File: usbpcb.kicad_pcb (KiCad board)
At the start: 2 copper layers, 32.5 x 56 mm, 6 parts, among them J1 USB_A, J2 USB3_A, J3 Conn_02x05_Counter_Clockwise, J4 Conn_02x05_Counter_Clockwise

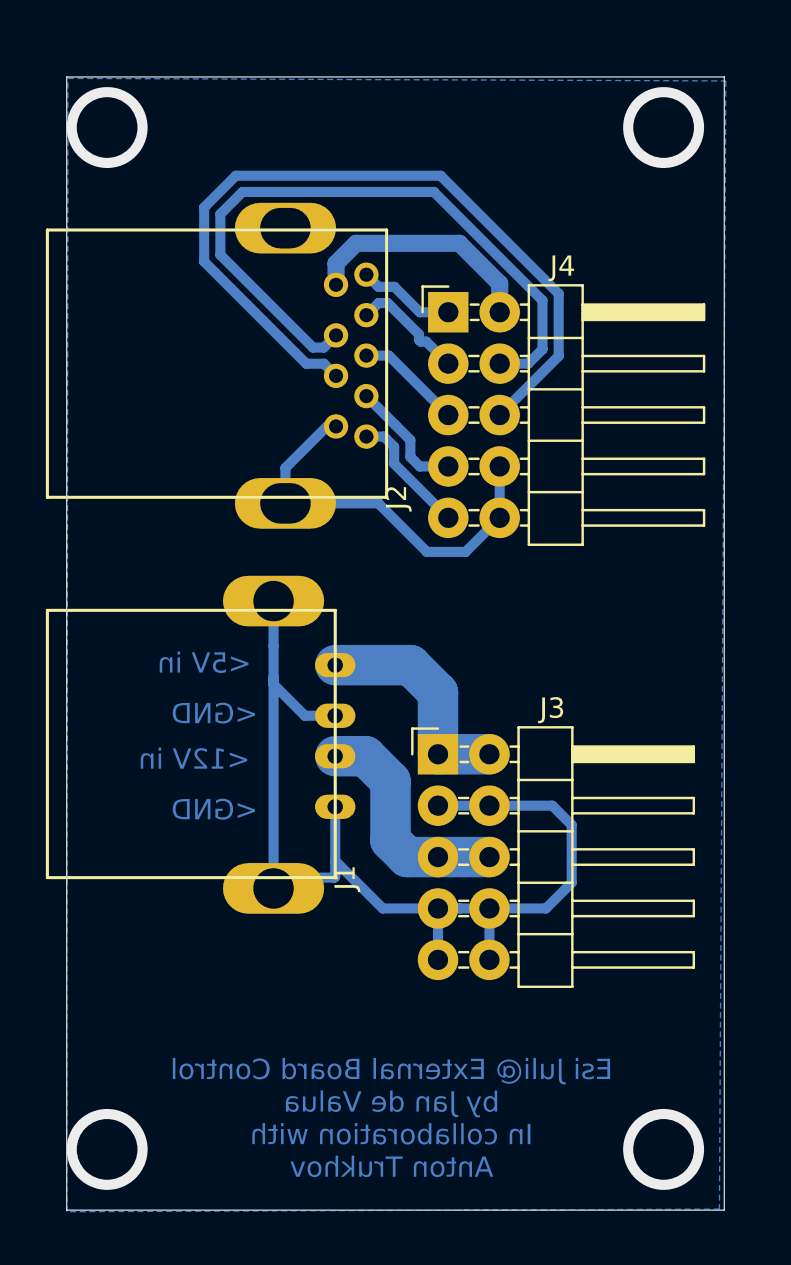
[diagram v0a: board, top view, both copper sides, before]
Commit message: update after fail
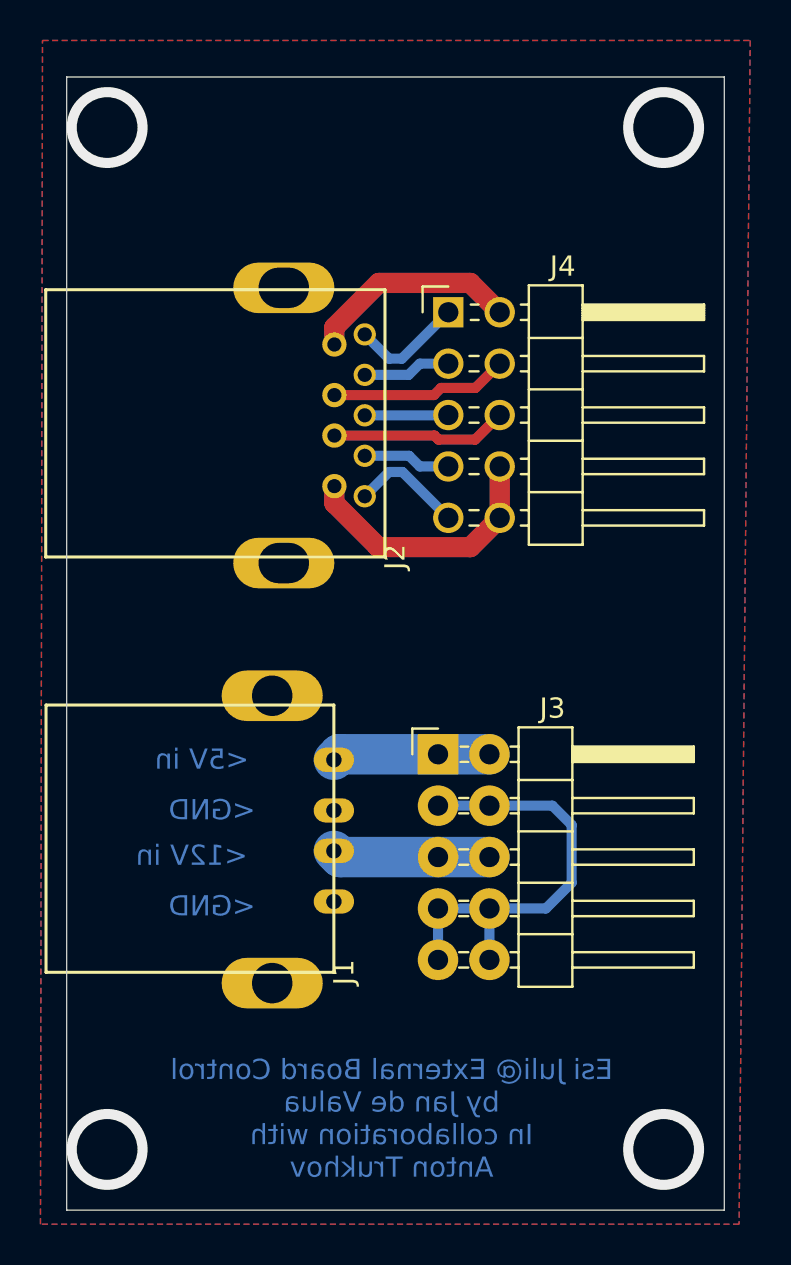
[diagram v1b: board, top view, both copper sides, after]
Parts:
- moved J1 4.68 mm to (44.1, 76.0)
- moved J2 2.95 mm to (46.7, 55.5)
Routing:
- net GND: track 72.6 -> 34.0 mm
- net /D_P: track 39.3 -> 8.76 mm
- net /D_N: track 33.3 -> 8.81 mm
- net /12V: track 11.4 -> 7.81 mm
- net /5V: track 11.2 -> 7.80 mm
- net /ST_N: track 5.98 -> 4.35 mm
- net /SR_P: track 5.70 -> 4.36 mm
- net Net-(J2-Pad1): track 11.8 -> 10.5 mm
- net Net-(J2-Pad7): track 5.26 -> 4.14 mm
- net /SR_N: track 4.82 -> 5.58 mm
- net /ST_P: track 6.23 -> 5.57 mm
- added copper zone on F.Cu, net GND
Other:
- net class Default removed
